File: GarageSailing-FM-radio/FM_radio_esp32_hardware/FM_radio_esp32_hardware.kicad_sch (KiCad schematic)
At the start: 39 parts, among them J1 AudioJack2_Ground_SwitchT, J2 Conn_01x06, J3 Conn_02x03_Odd_Even, J4 Conn_02x03_Odd_Even, SW1 SW_Push, SW2 SW_SPDT, SW3 SW_SPST, U1 ESP32-WROOM-32D, U2 RDA5807

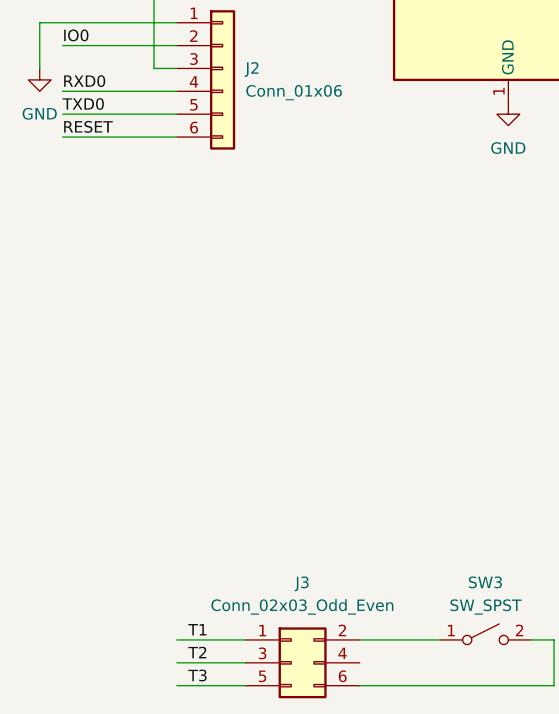
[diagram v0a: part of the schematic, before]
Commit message: Organize directories
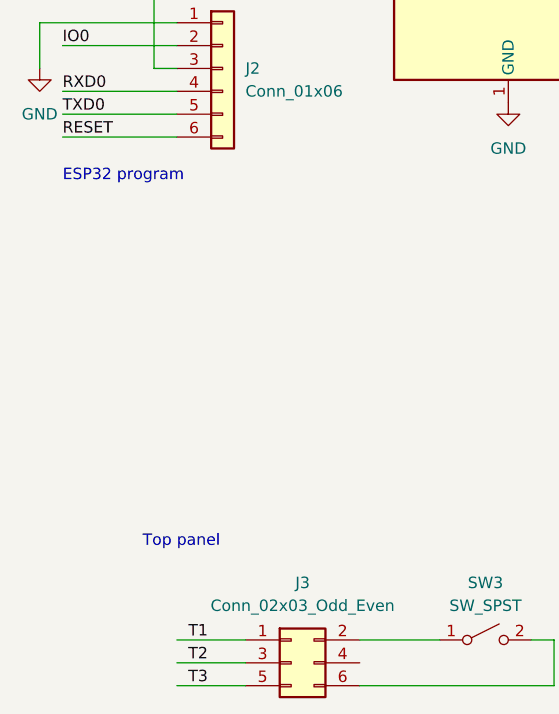
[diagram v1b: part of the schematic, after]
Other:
- note added: "ESP32 program"
- note added: "Top panel"
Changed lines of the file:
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@@
   (title_block
     (title "FM radio for GARAGE SAILING")
-    (date "2022-11-20")
-    (rev "v0.1.0")
+    (date "2022-11-26")
+    (rev "v1.0.0")
   )
   (junction (at 52.07 49.53) (diameter 0) (color 0 0 0 0)
@@
     (stroke (width 0) (type default) (color 0 0 0 0))
   )
+  (text "ESP32 program" (at 31.75 107.95 0)
+    (effects (font (size 1.27 1.27)) (justify left bottom))
+  )
+  (text "Top panel" (at 40.64 148.59 0)
+    (effects (font (size 1.27 1.27)) (justify left bottom))
+  )
   (label "VBAT" (at 265.43 35.56 0)

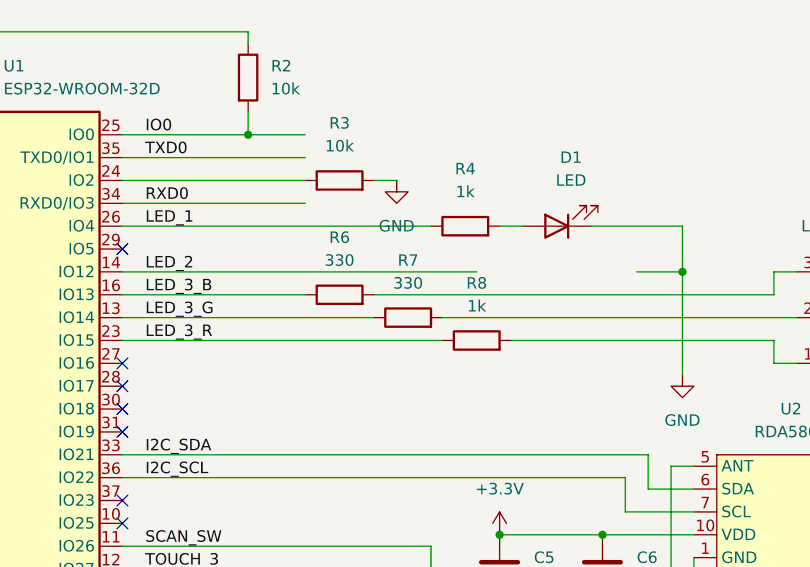
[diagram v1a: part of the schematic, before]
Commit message: Changed resistors value for the RGB LED.
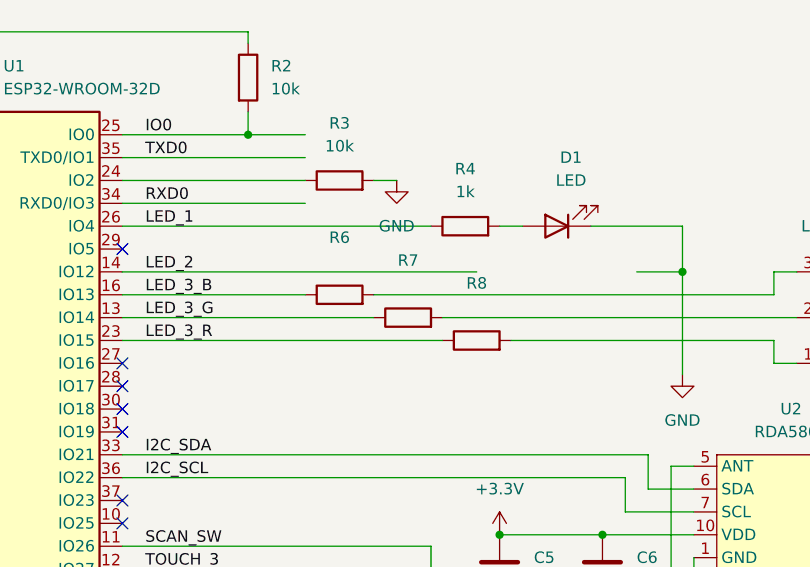
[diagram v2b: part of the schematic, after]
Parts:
- R6, R7: value 330 -> (none); footprint Resistor_SMD:R_0603_1608Metric -> (none)
- R8: value 1k -> (none); footprint Resistor_SMD:R_0603_1608Metric -> (none)
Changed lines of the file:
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@@
     (in_bom yes) (on_board yes) (fields_autoplaced)
     (property "Reference" "R8" (id 0) (at 135.89 49.53 90))
-    (property "Value" "1k" (id 1) (at 135.89 52.07 90))
-    (property "Footprint" "Resistor_SMD:R_0603_1608Metric" (id 2) (at 135.89 57.658 90)
+    (property "Value" "" (id 1) (at 135.89 52.07 90))
+    (property "Footprint" "" (id 2) (at 135.89 57.658 90)
       (effects (font (size 1.27 1.27)) hide)
     )
@@
     (in_bom yes) (on_board yes) (fields_autoplaced)
     (property "Reference" "R7" (id 0) (at 128.27 46.99 90))
-    (property "Value" "330" (id 1) (at 128.27 49.53 90))
-    (property "Footprint" "Resistor_SMD:R_0603_1608Metric" (id 2) (at 128.27 55.118 90)
+    (property "Value" "" (id 1) (at 128.27 49.53 90))
+    (property "Footprint" "" (id 2) (at 128.27 55.118 90)
       (effects (font (size 1.27 1.27)) hide)
     )
@@
     (in_bom yes) (on_board yes) (fields_autoplaced)
     (property "Reference" "R6" (id 0) (at 120.65 44.45 90))
-    (property "Value" "330" (id 1) (at 120.65 46.99 90))
-    (property "Footprint" "Resistor_SMD:R_0603_1608Metric" (id 2) (at 120.65 52.578 90)
+    (property "Value" "" (id 1) (at 120.65 46.99 90))
+    (property "Footprint" "" (id 2) (at 120.65 52.578 90)
       (effects (font (size 1.27 1.27)) hide)
     )
@@
     )
     (path "/faaee96f-1cf0-4bf5-8d46-7e90745cc769"
-      (reference "R6") (unit 1) (value "330") (footprint "Resistor_SMD:R_0603_1608Metric")
+      (reference "R6") (unit 1) (value "220") (footprint "Resistor_SMD:R_0603_1608Metric")
     )
     (path "/7348369c-b81b-45f2-af1e-23f8b53e2b15"
-      (reference "R7") (unit 1) (value "330") (footprint "Resistor_SMD:R_0603_1608Metric")
+      (reference "R7") (unit 1) (value "2k") (footprint "Resistor_SMD:R_0603_1608Metric")
     )
     (path "/53b3d478-aede-49e5-a9c6-af0d51081e6b"
-      (reference "R8") (unit 1) (value "1k") (footprint "Resistor_SMD:R_0603_1608Metric")
+      (reference "R8") (unit 1) (value "470") (footprint "Resistor_SMD:R_0603_1608Metric")
     )
     (path "/f9679bf7-9b73-4183-8072-4655075ba7d7"

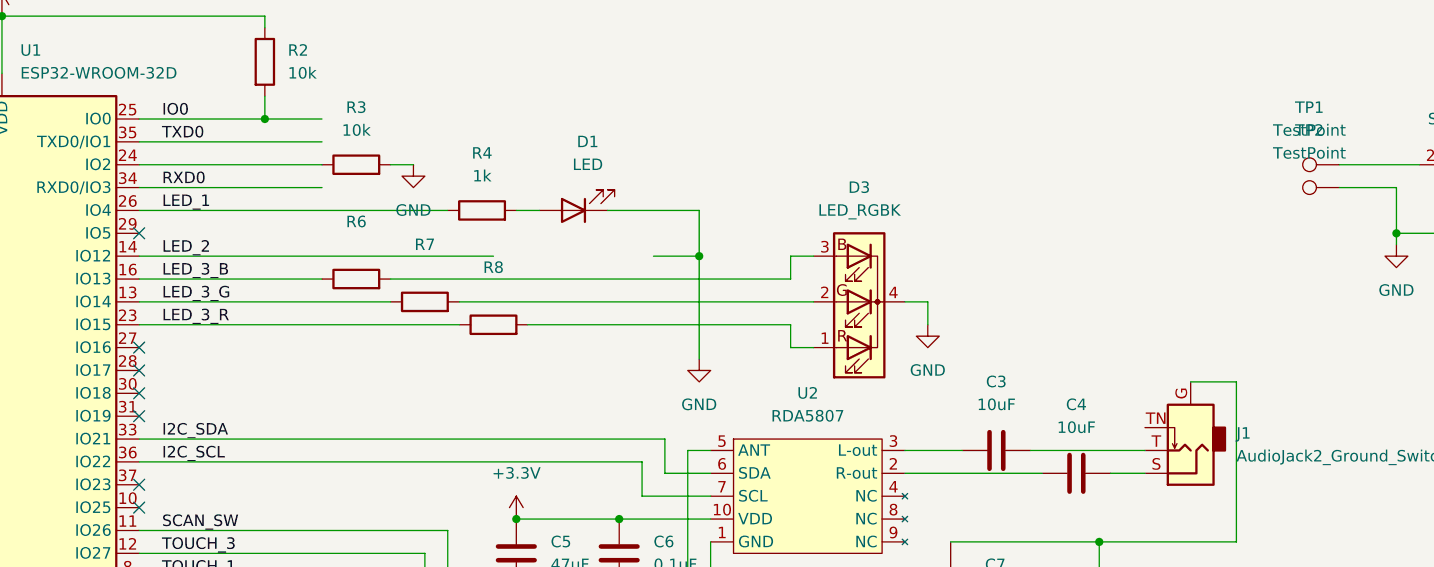
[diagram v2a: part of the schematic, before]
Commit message: RGB led pin arrangements hacks
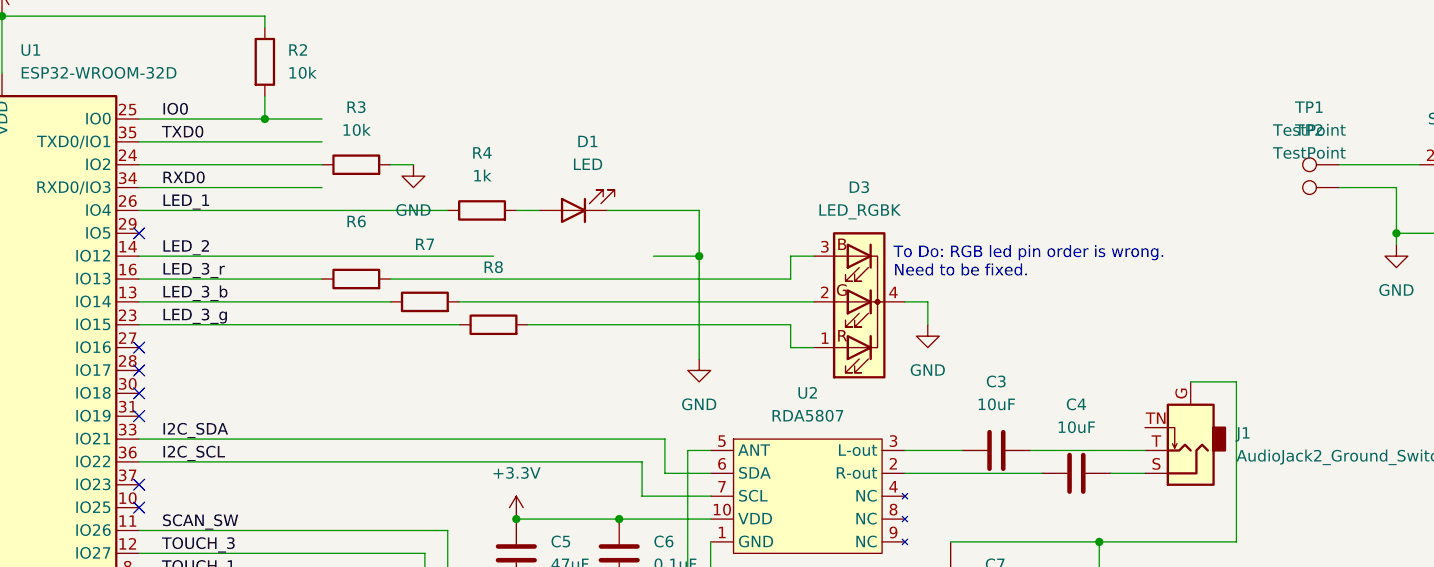
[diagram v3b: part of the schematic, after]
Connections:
- net LED_3_B renamed LED_3_r
- net LED_3_G renamed LED_3_b
- net LED_3_R renamed LED_3_g
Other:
- note added: "To Do: RGB led pin order is wrong. Need to be fixed."
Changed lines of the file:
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@@
     (stroke (width 0) (type default) (color 0 0 0 0))
   )
+  (text "To Do: RGB led pin order is wrong. \nNeed to be fixed."
+    (at 180.34 50.8 0)
+    (effects (font (size 1.27 1.27)) (justify left bottom))
+  )
   (text "ESP32 program" (at 31.75 107.95 0)
     (effects (font (size 1.27 1.27)) (justify left bottom))
@@
     (effects (font (size 1.27 1.27)) (justify left bottom))
   )
-  (label "LED_3_B" (at 99.06 50.8 0)
+  (label "LED_3_r" (at 99.06 50.8 0)
     (effects (font (size 1.27 1.27)) (justify left bottom))
   )
@@
     (effects (font (size 1.27 1.27)) (justify left bottom))
   )
-  (label "LED_3_G" (at 99.06 53.34 0)
+  (label "LED_3_b" (at 99.06 53.34 0)
     (effects (font (size 1.27 1.27)) (justify left bottom))
   )
@@
     (effects (font (size 1.27 1.27)) (justify left bottom))
   )
-  (label "LED_3_R" (at 99.06 55.88 0)
+  (label "LED_3_g" (at 99.06 55.88 0)
     (effects (font (size 1.27 1.27)) (justify left bottom))
   )
@@
     )
     (path "/faaee96f-1cf0-4bf5-8d46-7e90745cc769"
-      (reference "R6") (unit 1) (value "220") (footprint "Resistor_SMD:R_0603_1608Metric")
+      (reference "R6") (unit 1) (value "470") (footprint "Resistor_SMD:R_0603_1608Metric")
     )
     (path "/7348369c-b81b-45f2-af1e-23f8b53e2b15"
-      (reference "R7") (unit 1) (value "2k") (footprint "Resistor_SMD:R_0603_1608Metric")
+      (reference "R7") (unit 1) (value "220") (footprint "Resistor_SMD:R_0603_1608Metric")
     )
     (path "/53b3d478-aede-49e5-a9c6-af0d51081e6b"
-      (reference "R8") (unit 1) (value "470") (footprint "Resistor_SMD:R_0603_1608Metric")
+      (reference "R8") (unit 1) (value "2k") (footprint "Resistor_SMD:R_0603_1608Metric")
     )
     (path "/f9679bf7-9b73-4183-8072-4655075ba7d7"
